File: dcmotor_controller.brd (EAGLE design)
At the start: 142.2 x 90.6 mm, 81 parts, among them IC1 L298, IC2 L298, IC5 SN74LVCR162245A, Q1 MOSFET-PCHANNEL_SOT23-3, Q2 8MHz, T1 BC857BS, T14 BSS306N, U2 STM32F10XRXT6

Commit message: Add files via upload
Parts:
- moved C27 1.27 mm to (100.3, 46.7)
- moved R7 1.02 mm to (55.6, 38.1)
- moved C28 0.51 mm to (87.4, 46.7), turned to 0 degrees
- moved C16 0.25 mm to (93.7, 26.9)
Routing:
- net 3V3: track 285.2 -> 325.5 mm, vias 9 -> 10
- net CLK: track 134.2 -> 115.5 mm
- net GND: track 895.7 -> 877.8 mm, vias 6 -> 4
- net SPI1_NSS: track 97.2 -> 112.3 mm, vias 4 -> 3
- net RPI_RXD: track 80.7 -> 92.5 mm, vias 2 -> 1
- net BOOTO: track 29.7 -> 35.5 mm
- net INDEX_W1: track 46.6 -> 42.2 mm, vias 2 -> 1
- net SWCLK: track 74.0 -> 78.3 mm
- net RPI_CLK: track 81.0 -> 84.9 mm, vias 5 -> 1
- net B_DIR_V1: track 40.4 -> 37.6 mm
- net IN11_UC: track 25.9 -> 28.6 mm
- net IN12_UC: track 26.4 -> 29.1 mm
- net INDEX_W4: track 58.1 -> 60.7 mm
- net IN21_UC: track 30.6 -> 33.2 mm
- net A_LSB_U4: track 57.6 -> 60.1 mm
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- removed copper zone on layer 1, net GND
- removed copper zone on layer 16, net GND

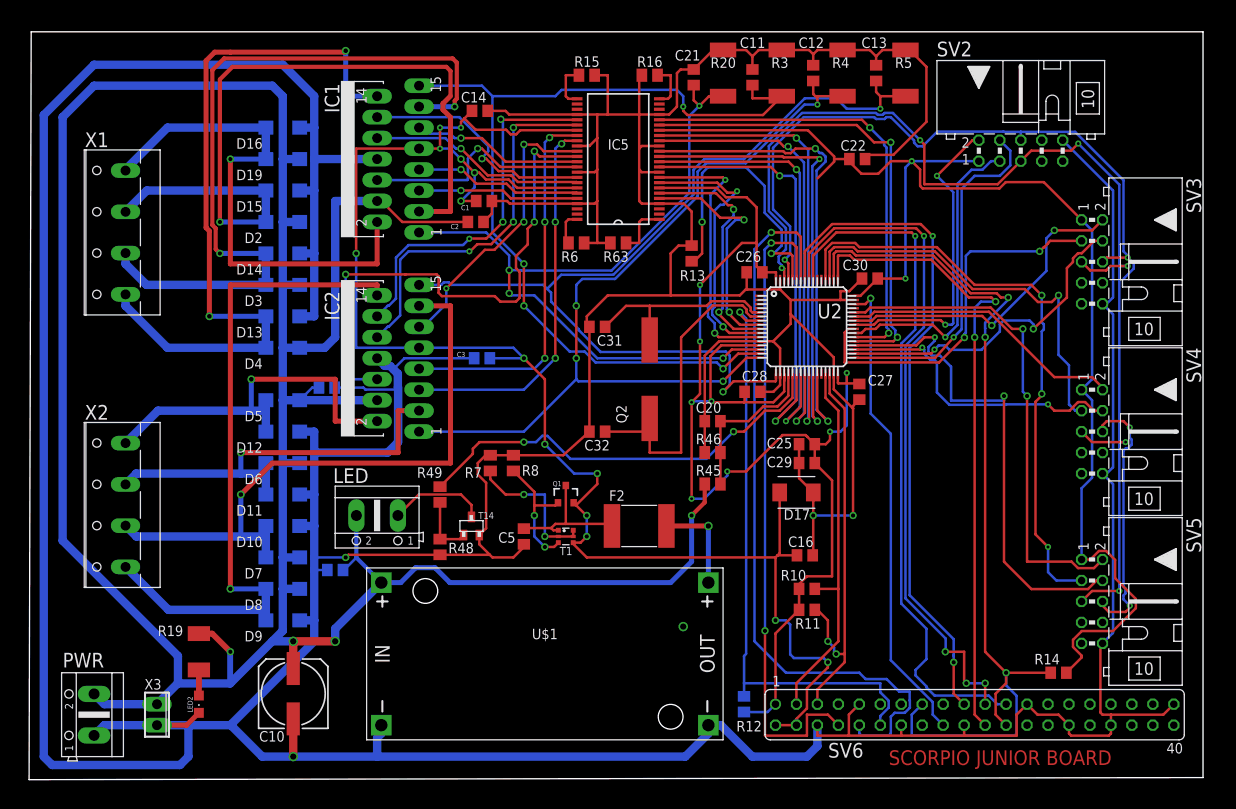
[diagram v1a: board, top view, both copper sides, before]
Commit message: some drc rules, airwires repaired and schemat checked
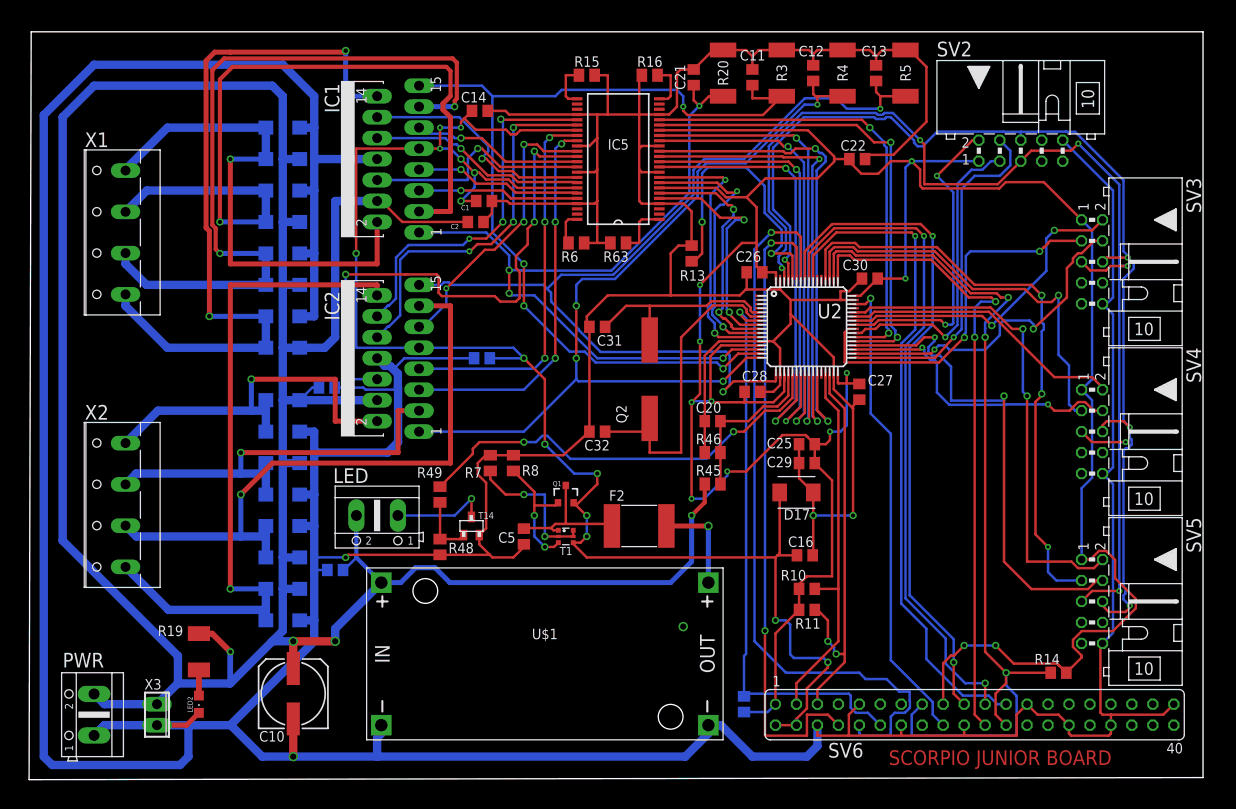
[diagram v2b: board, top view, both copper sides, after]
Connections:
- removed net +3V3: SV6.17
- net 3V3: now also SV6.17
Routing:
- net 3V3: track 325.5 -> 357.2 mm, vias 10 -> 12
- net CLK: track 115.5 -> 133.8 mm
- net NRST: track 72.4 -> 69.1 mm
- net RPI_CLK: track 84.9 -> 81.8 mm
- net RPI_MISO: track 83.1 -> 81.8 mm, vias 4 -> 2
- net N$24: track 11.9 -> 12.0 mm, vias 0 -> 1

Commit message: Add files via upload
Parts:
- removed C22: 100n, resistor:C0805
- removed IC5: SN74LVCR162245A, texas:DL_R-PDSO-G48
- removed R15, R16, R6, R63: 10k, resistor:M0805
- added C6, C7, C8: 100n, resistor:C0805
- added R1, R62: 10k, resistor:M0805
- added U1, U3: SN74LVC4245APWR, Texas Instruments_By_element14_Batch_1:SOP65P640X120-24N
- moved C14 17.5 mm to (71.6, 83.6), turned to 90 degrees
- moved C1 14.4 mm to (42.2, 63.0), turned to 270 degrees
- moved C2 10.1 mm to (44.7, 63.0), turned to 270 degrees
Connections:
- removed net N$7: IC5.25, R15.2
- removed net N$8: IC5.48, R6.2
- removed net N$9: IC5.1, R63.1
- new net N$5: R1.1, U3.2, U3.22
- net 3V3: now also C14.1, C7.1, U1.23, U1.24, U3.23, U3.24; no longer C22.2, IC5.18, IC5.7
- net 5V: now also C6.1, C8.1, U1.1, U3.1; no longer C14.2, IC5.31, IC5.42
- net EN1_UC: now also U1.21; no longer IC5.11
- net EN2_UC: now also U1.20; no longer IC5.12
- net EN3_UC: now also U1.19; no longer IC5.13
- net EN4_UC: now also U1.18; no longer IC5.14
- net GND: now also C14.2, C6.2, C7.2, C8.2, R1.2, R62.2, U1.11, U1.12, U1.13, U3.11, U3.12, U3.13; no longer C14.1, C22.1, IC5.10, IC5.15, IC5.21, IC5.28, IC5.34, IC5.39, IC5.4, IC5.45, R15.1, R16.2, R6.1, R63.2
- net IN11: now also U3.3; no longer IC5.44
- net IN11_UC: now also U3.21; no longer IC5.5
- net IN12: now also U3.4; no longer IC5.43
- net IN12_UC: now also U3.20; no longer IC5.6
- net IN21: now also U3.5; no longer IC5.41
- net IN21_UC: now also U3.19; no longer IC5.8
- net IN22: now also U3.6; no longer IC5.40
- net IN22_UC: now also U3.18; no longer IC5.9
- net IN31: now also U1.7; no longer IC5.33
- net IN31_UC: now also U1.17; no longer IC5.16
- net IN32: now also U1.8; no longer IC5.32
- net IN32_UC: now also U1.16; no longer IC5.17
- net IN41: now also U1.9; no longer IC5.30
- net IN41_UC: now also U1.15; no longer IC5.19
- net IN42: now also U1.10; no longer IC5.29
- net IN42_UC: now also U1.14; no longer IC5.20
- net N$4: now also R62.1, U1.2, U1.22; no longer IC5.24, R16.1
- net PWM_SIGNAL1: now also U1.3; no longer IC5.38
- net PWM_SIGNAL2: now also U1.4; no longer IC5.37
- net PWM_SIGNAL3: now also U1.5; no longer IC5.36
- net PWM_SIGNAL4: now also U1.6; no longer IC5.35
- net SCL: now also U2.29; no longer U2.30
- net SDA: now also U2.30; no longer U2.29
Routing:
- net GND: track 877.8 -> 834.2 mm, vias 4 -> 6
- net N$4: track 5.63 -> 22.5 mm, vias 0 -> 2
- net PWM_SIGNAL1: track 28.2 -> 42.8 mm
- net PWM_SIGNAL3: track 64.6 -> 50.4 mm, vias 3 -> 0
- net IN31_UC: track 56.5 -> 67.0 mm
- net 24V: track 352.9 -> 343.2 mm
- net IN32_UC: track 57.5 -> 66.7 mm
- net N$5: track 0.00 -> 8.95 mm
- net IN21: track 26.5 -> 34.8 mm
- net 3V3: track 357.2 -> 348.9 mm, vias 12 -> 15
- net IN22: track 29.2 -> 36.6 mm
- net IN12: track 20.3 -> 27.2 mm
- net N$9: track 6.70 -> 0.00 mm
- net EN1_UC: track 54.3 -> 60.9 mm
- net IN22_UC: track 33.6 -> 27.3 mm
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
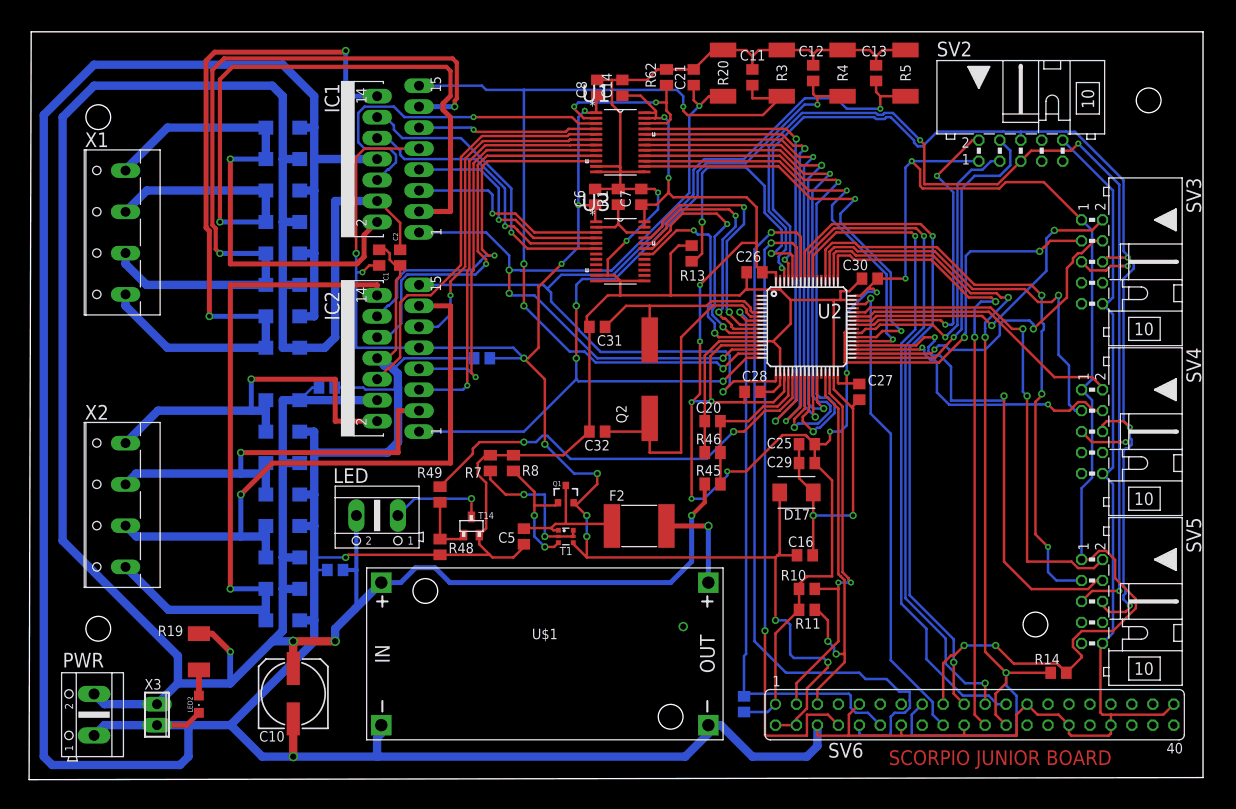
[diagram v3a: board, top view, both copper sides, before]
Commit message: rpi header repaired
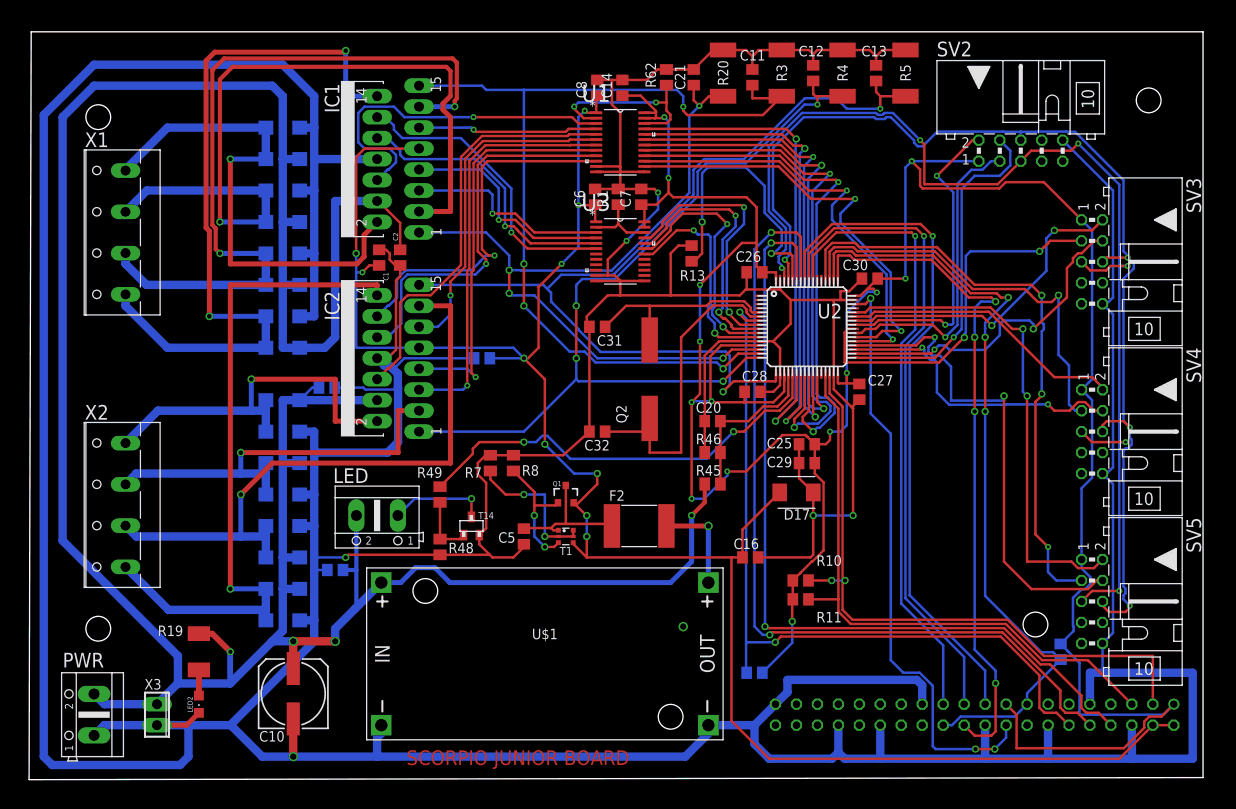
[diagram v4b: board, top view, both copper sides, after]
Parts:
- moved C16 6.61 mm to (87.1, 26.7)
- moved R12 4.02 mm to (87.6, 12.7), turned to 180 degrees
- moved R14 2.55 mm to (124.7, 15.2), flipped to the bottom, turned to 90 degrees
- moved R11 1.48 mm to (93.2, 21.6)
- moved R10 1.27 mm to (93.2, 23.9)
- flipped SV6 to the bottom
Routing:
- net GND: track 834.2 -> 892.0 mm
- net 5V: track 197.6 -> 239.9 mm, vias 12 -> 10
- net SDA: track 47.6 -> 79.7 mm
- net NRST: track 69.1 -> 93.2 mm, vias 1 -> 2
- net SCL: track 50.0 -> 73.3 mm, vias 2 -> 0
- net RPI_TXD: track 79.2 -> 101.8 mm
- net SPI1_NSS: track 112.3 -> 94.7 mm
- net SWDIO: track 57.7 -> 72.0 mm, vias 1 -> 3
- net RPI_RXD: track 92.5 -> 104.7 mm, vias 1 -> 2
- net SWCLK: track 78.3 -> 84.1 mm, vias 2 -> 4
- net RPI_CLK: track 81.8 -> 76.2 mm
- net 3V3: track 348.9 -> 352.1 mm, vias 15 -> 14
- net RPI_MISO: track 81.8 -> 79.4 mm, vias 2 -> 1
- net RPI_MOSI: track 81.5 -> 82.6 mm, vias 2 -> 1

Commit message: Add files via upload
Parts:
- added C15, C17: 100n, resistor:C0805
- added C18, C19: 10u, resistor:153CLV-0807
- added U4: MCP1825S-3302E/DB, MCP1825S-3302E_DB:SOT230P700X180-4N
- moved C9 1.85 mm to (37.3, 23.4), turned to 270 degrees
- moved C4 0.51 mm to (35.8, 47.8)
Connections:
- net 3V3: now also C17.1, C19.+, U4.3; no longer SV6.1, SV6.17
- net 5V: now also C15.1, C18.+, U4.1
- net D01: now also U2.53
- net D02: now also U2.2
- net D03: now also U2.3
- net D04: now also U2.4
- net GND: now also C15.2, C17.2, C18.-, C19.-, U4.2, U4.4
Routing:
- net D04: track 0.00 -> 134.2 mm, vias 0 -> 4
- net D03: track 0.00 -> 109.7 mm, vias 0 -> 4
- net GND: track 892.0 -> 967.4 mm, vias 6 -> 7
- net D02: track 0.00 -> 70.8 mm, vias 0 -> 3
- net 5V: track 239.9 -> 285.1 mm, vias 10 -> 12
- net D01: track 0.00 -> 38.9 mm, vias 0 -> 1
- net 3V3: track 352.1 -> 340.9 mm, vias 14 -> 15
- net 24V: track 343.2 -> 339.7 mm
- net IN22_UC: track 27.3 -> 29.0 mm
- net IN21_UC: track 31.2 -> 32.7 mm
- net NRST: track 93.2 -> 94.2 mm
- net RPI_MISO: track 79.4 -> 80.0 mm
- net OSC_OUT: track 40.8 -> 40.2 mm
- net OSC_IN: track 25.0 -> 24.4 mm
